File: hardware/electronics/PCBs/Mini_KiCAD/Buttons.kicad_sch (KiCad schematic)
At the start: 5 parts

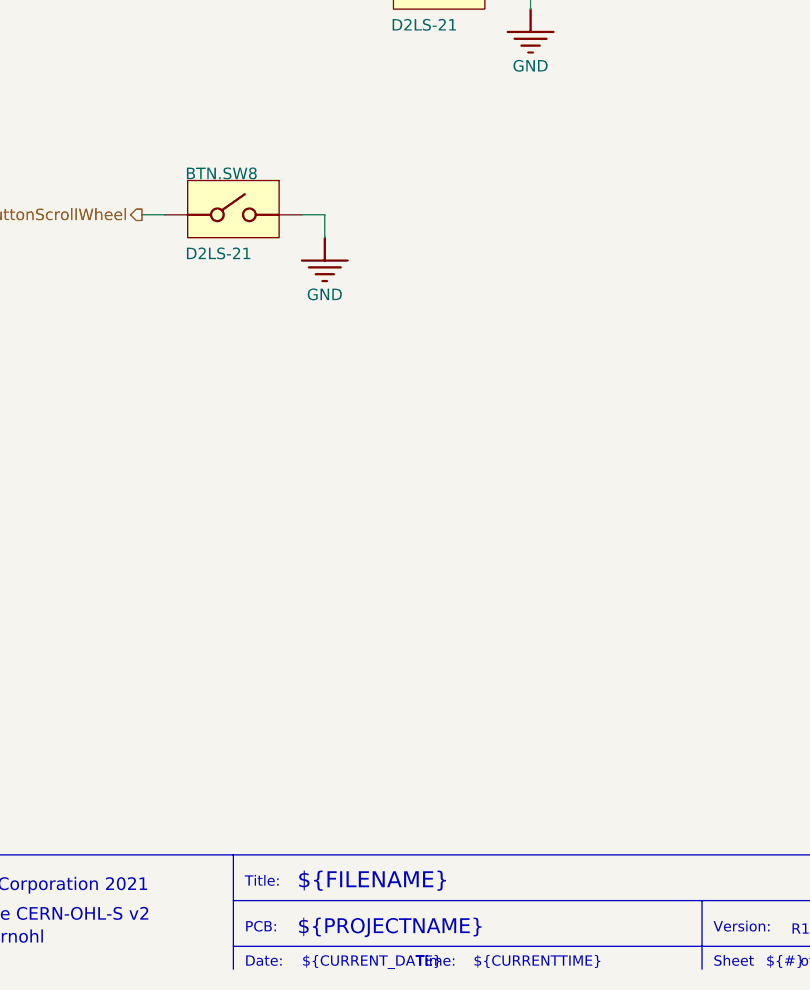
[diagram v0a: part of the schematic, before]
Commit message: Initial commit of the modified Ploopy Mini PCB with RP2040, PMW3360 and mid-mounted USB-C
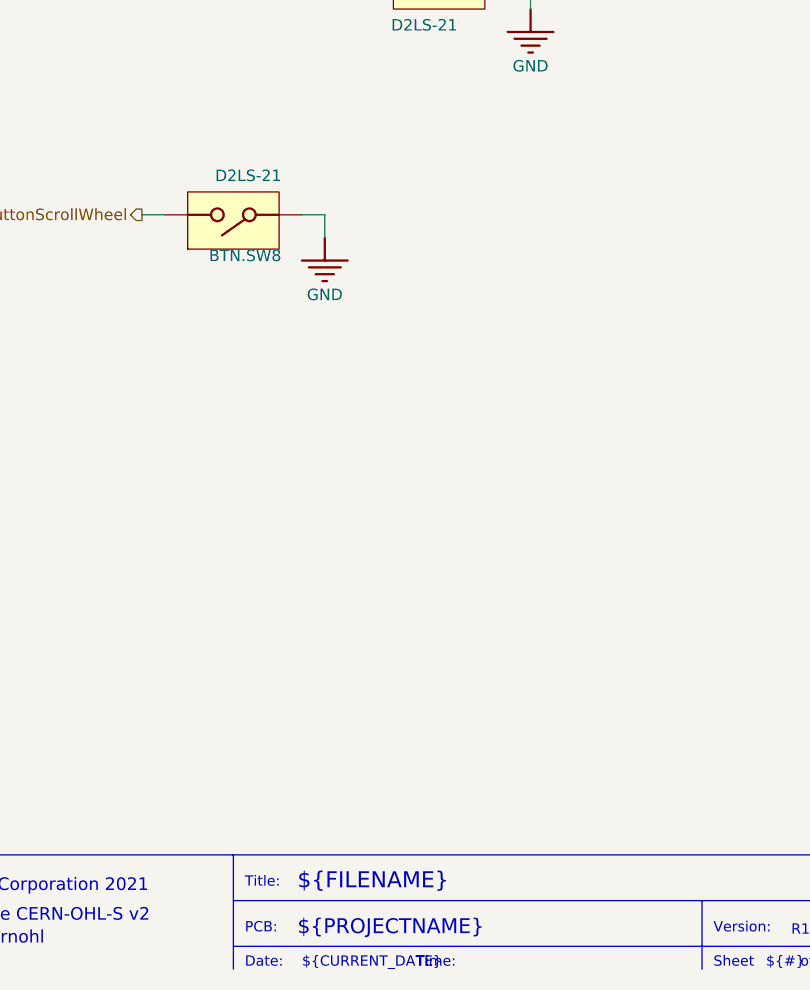
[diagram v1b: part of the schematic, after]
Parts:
- BTN.SW1, BTN.SW2, BTN.SW5, BTN.SW7, BTN.SW8: footprint D2LS-21 -> Switches.PcbLib:D2LS-21
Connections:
- net ButtonScrollWheel: now also BTN.SW8.B; no longer BTN.SW8.A
- net GND: now also BTN.SW8.A; no longer BTN.SW8.B
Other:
- note removed: "${CURRENTTIME}"
- moved on the sheet: BTN.SW8
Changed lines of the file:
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@@
-		)
-	)
-	(text "${CURRENTTIME}"
-		(exclude_from_sim no)
-		(at 194.31 210.82 0)
-		(effects
-			(font
-				(size 1.143 1.143)
-			)
-			(justify left bottom)
 		)
 	)
@@
 	(symbol
 		(lib_id "Mini-altium-import:BTN_0_D2LS-21")
-		(at 167.64 127 0)
+		(at 167.64 127 180)
 		(unit 1)
 		(exclude_from_sim no)
@@
 		(dnp no)
 		(property "Reference" "BTN.SW8"
-			(at 162.306 123.19 0)
+			(at 172.974 130.81 0)
 			(effects
 				(font
@@
 		)
 		(property "Value" "D2LS-21"
-			(at 162.306 132.08 0)
-			(effects
-				(font
-					(size 1.27 1.27)
-				)
-				(justify left bottom)
-			)
-		)
-		(property "Footprint" "D2LS-21"
+			(at 172.974 121.92 0)
+			(effects
+				(font
+					(size 1.27 1.27)
+				)
+				(justify left bottom)
+			)
+		)
+		(property "Footprint" "Switches.PcbLib:D2LS-21"
 			(at 167.64 127 0)
 			(effects
@@
 		)
 		(property "SUPPLIER 1" "Digi-Key"
-			(at 159.512 123.19 0)
+			(at 175.768 130.81 0)
 			(effects
 				(font
@@
 		)
 		(property "SUPPLIER 2" "Mouser"
-			(at 159.512 120.65 0)
+			(at 175.768 133.35 0)
 			(effects
 				(font
@@
 		)
 		(property "SUPPLIER PART NUMBER 1" "Z4378CT-ND"
-			(at 159.512 123.19 0)
+			(at 175.768 130.81 0)
 			(effects
 				(font
@@
 		)
 		(property "SUPPLIER PART NUMBER 2" "653-D2LS-21"
-			(at 159.512 120.65 0)
+			(at 175.768 133.35 0)
 			(effects
 				(font
@@
 			)
 		)
-		(property "Footprint" "D2LS-21"
+		(property "Footprint" "Switches.PcbLib:D2LS-21"
 			(at 190.5 101.6 0)
 			(effects
@@
 			)
 		)
-		(property "Footprint" "D2LS-21"
+		(property "Footprint" "Switches.PcbLib:D2LS-21"
 			(at 114.3 101.6 0)
 			(effects
@@
 			)
 		)
-		(property "Footprint" "D2LS-21"
+		(property "Footprint" "Switches.PcbLib:D2LS-21"
 			(at 114.3 76.2 0)
 			(effects
@@
 			)
 		)
-		(property "Footprint" "D2LS-21"
+		(property "Footprint" "Switches.PcbLib:D2LS-21"
 			(at 190.5 76.2 0)
 			(effects

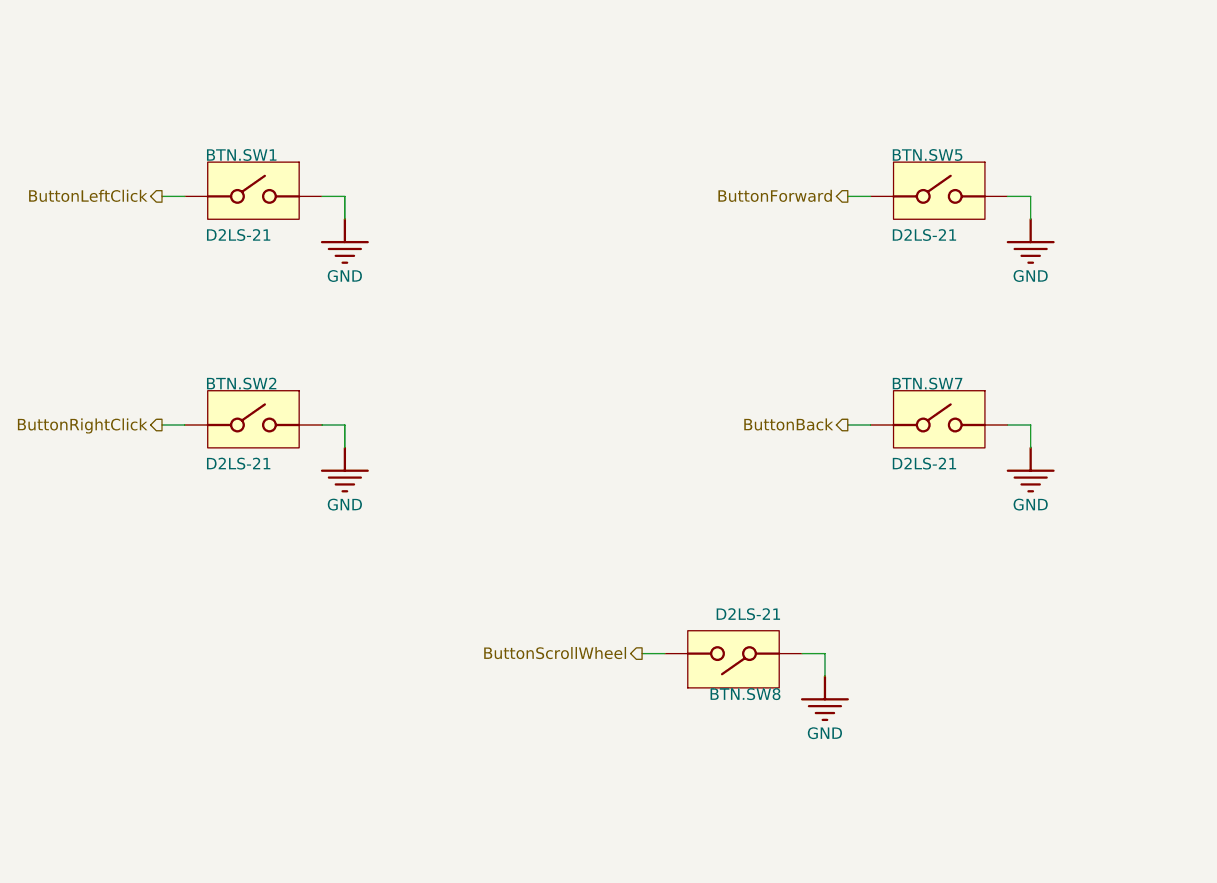
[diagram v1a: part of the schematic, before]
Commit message: Rev1.002 Replaced all symbols in the schematic with built-in symbols where applicable. Reoriented the sensor to solve interference and tracking issues. Replaced the mid-mount USB port with regular port.
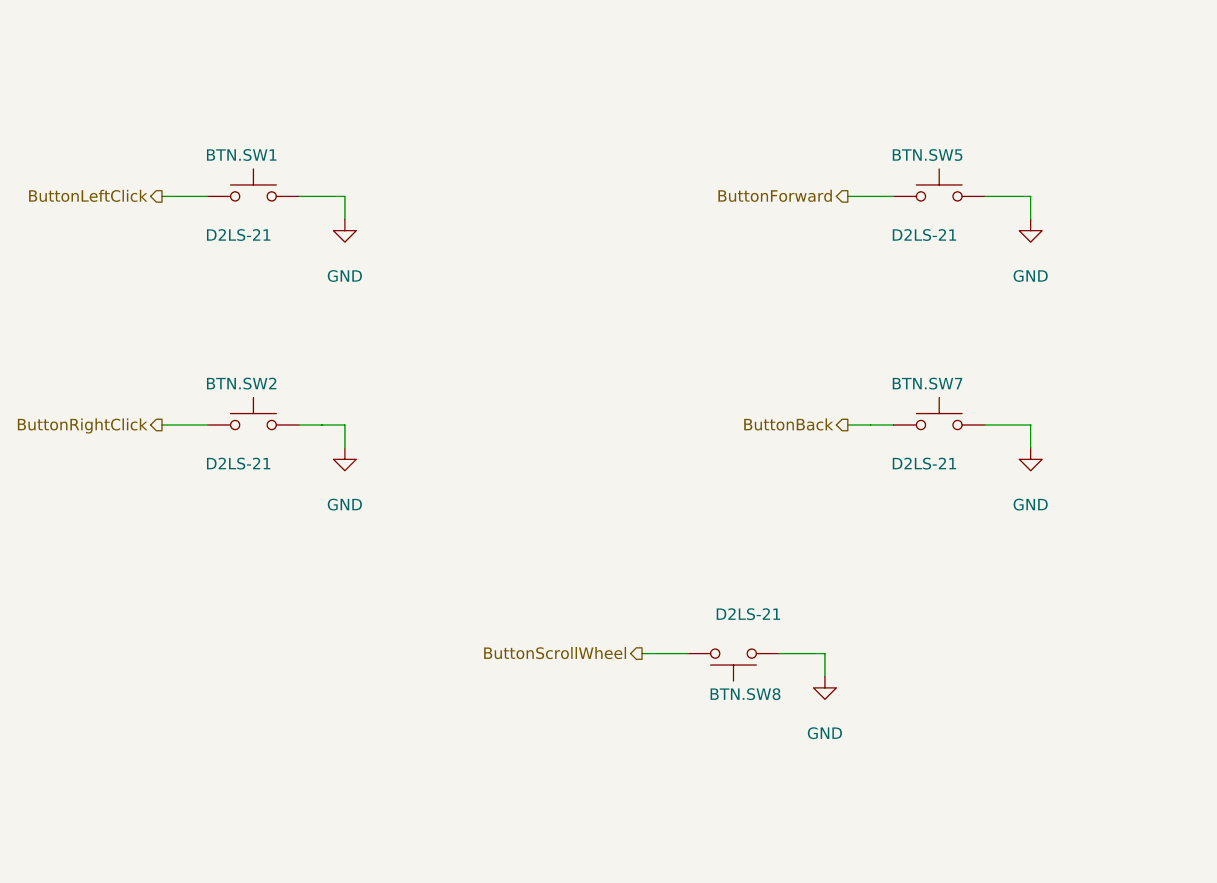
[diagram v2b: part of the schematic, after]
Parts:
- BTN.SW1, BTN.SW2, BTN.SW5, BTN.SW7, BTN.SW8: symbol Mini-altium-import:BTN_0_D2LS-21 -> Switch:SW_Push
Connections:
- net ButtonBack: now also BTN.SW7.1; no longer BTN.SW7.A
- net ButtonForward: now also BTN.SW5.1; no longer BTN.SW5.A
- net ButtonLeftClick: now also BTN.SW1.1; no longer BTN.SW1.A
- net ButtonRightClick: now also BTN.SW2.1; no longer BTN.SW2.A
- net ButtonScrollWheel: now also BTN.SW8.2; no longer BTN.SW8.B
- net GND: now also BTN.SW1.2, BTN.SW2.2, BTN.SW5.2, BTN.SW7.2, BTN.SW8.1; no longer BTN.SW1.B, BTN.SW2.B, BTN.SW5.B, BTN.SW7.B, BTN.SW8.A
